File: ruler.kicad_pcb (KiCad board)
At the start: 2 copper layers, 170.8 x 38.1 mm, 80 parts, among them J1 USB_OTG, Q1 SOT23, Q2 SOT323, Q3 SOT883, Q4 SOT523, Q5 SOT223, Q6 SOT89, Q7 SuperSOT, SW1 KMR2, SW2 EVQPE1, SW3 B3U1000P, SW4 FSMCT, SW5 TL3315, SW6 FSM2JSM, SW7 JS202011SCQN, U1 QFN-0.5mm, U10 SOT963-6, U11 SSOP14, U12 SO16-L, U13 SOT666, U14 SOT1194, U15 SOT1333, U16 SOT669, U17 TSSOP 4.4x3mm, U18 SO4, U19 VSSOP, U2 LQFP, U3 SOIC, U4 BGA-0.8mm, U5 TSSOP 3x3mm, U6 MSOIC, U7 TSOP-0.95mm, U8 SOT23-6, U9 SOT23-8

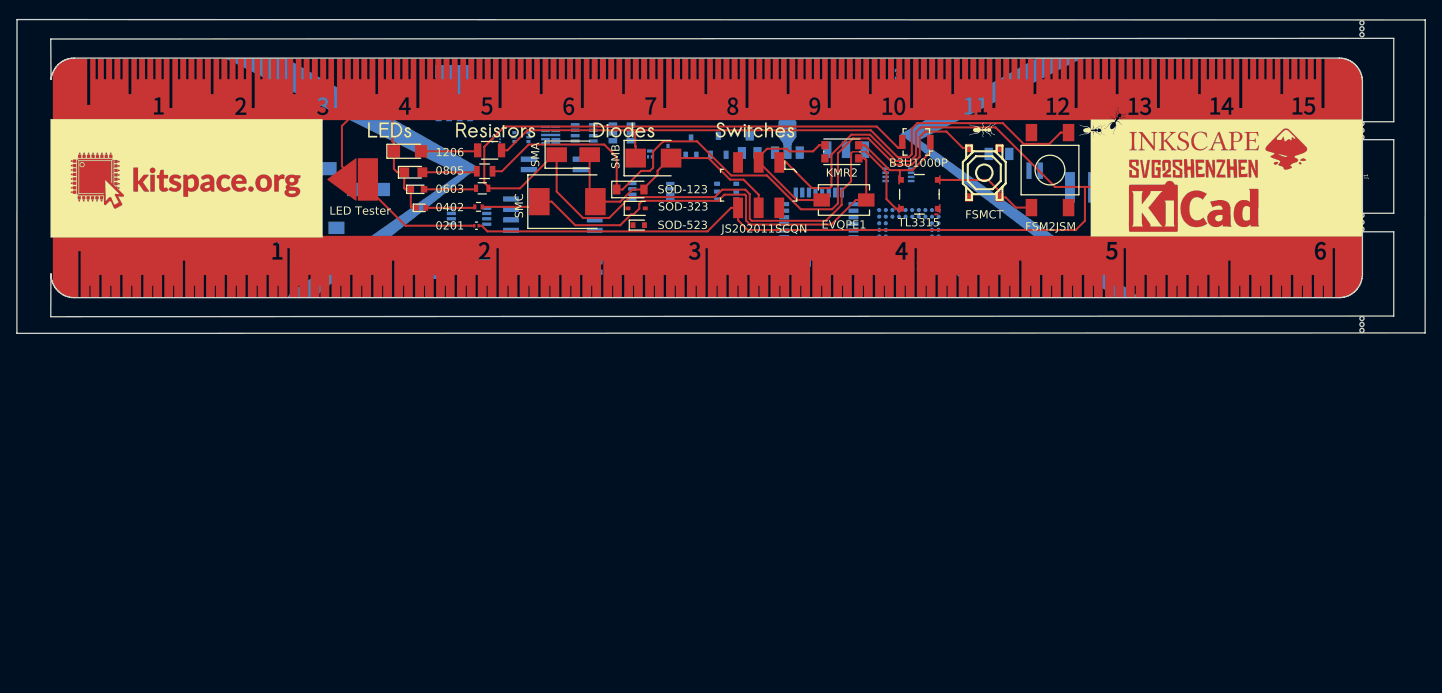
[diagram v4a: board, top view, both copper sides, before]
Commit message: Panelize two rulers
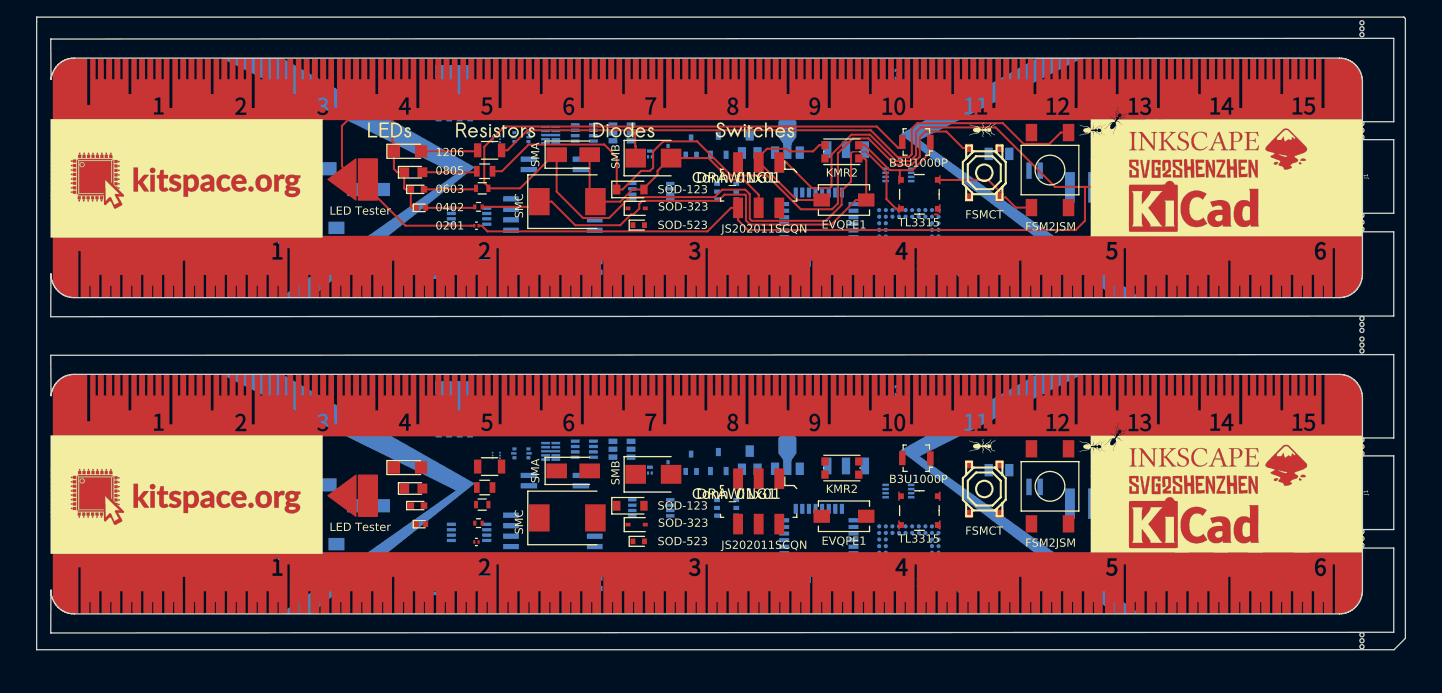
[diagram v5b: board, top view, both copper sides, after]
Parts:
- added C1: 3x5.3mm, KiCad/Capacitors_SMD.pretty:CP_Elec_3x5.3, B.Cu at (103.9, 144.8)
- added C2: 4x5.8mm, KiCad/Capacitors_SMD.pretty:CP_Elec_4x5.8, B.Cu at (96.9, 142.3)
- added C3: 5x5.8mm, KiCad/Capacitors_SMD.pretty:CP_Elec_5x5.8, B.Cu at (88.6, 140.0)
- added C4: 8x10mm, KiCad/Capacitors_SMD.pretty:CP_Elec_8x10, B.Cu at (78.2, 138.2)
- added C5: A/3216, KiCad/Capacitors_Tantalum_SMD.pretty:CP_Tantalum_Case-A_EIA-3216-18_Reflow, B.Cu at (98.6, 149.4)
- added C6: B/3528, KiCad/Capacitors_Tantalum_SMD.pretty:CP_Tantalum_Case-B_EIA-3528-21_Reflow, B.Cu at (92.3, 150.1)
- added C7: C/6032, KiCad/Capacitors_Tantalum_SMD.pretty:CP_Tantalum_Case-C_EIA-6032-28_Reflow, B.Cu at (84.6, 150.6)
- added C8: D/7343, KiCad/Capacitors_Tantalum_SMD.pretty:CP_Tantalum_Case-D_EIA-7343-31_Reflow, B.Cu at (74.9, 151.1)
- added D1: SMA, KiCad/Diodes_SMD.pretty:D_SMA, F.Cu at (128.7, 140.6)
- added D2: SMB, KiCad/Diodes_SMD.pretty:D_SMB, F.Cu at (138.4, 141.0)
- added D3: SMC, KiCad/Diodes_SMD.pretty:D_SMC, F.Cu at (128.0, 146.3)
- added D4: SOD-123, KiCad/Diodes_SMD.pretty:D_SOD-123, F.Cu at (135.6, 144.8)
- added D5: SOD-323, KiCad/Diodes_SMD.pretty:D_SOD-323, F.Cu at (136.4, 147.1)
- added D6: SOD-523, KiCad/Diodes_SMD.pretty:D_SOD-523, F.Cu at (136.7, 149.1)
- added DRAWING1: Conn_01x01, drawings:ruler, F.Cu at (148.5, 143.4)
- added DRAWING10: Conn_01x01, drawings:tantalum_text, B.Cu at (68.6, 152.7)
- added DRAWING11: Conn_01x01, drawings:electrolytic_text, B.Cu at (71.6, 139.4)
- added DRAWING12: Conn_01x01, drawings:vscore, B.Cu at (65.3, 136.4)
- added DRAWING13: Conn_01x01, drawings:mouse_bites, B.Cu at (213.4, 132.1)
- added DRAWING14: Conn_01x01, drawings:mouse, B.Cu at (188.7, 139.2)
- added DRAWING15: Conn_01x01, drawings:chipmunk, B.Cu at (202.7, 134.9)
- added DRAWING16: Conn_01x01, drawings:weasel, B.Cu at (214.4, 136.9)
- added DRAWING17: Conn_01x01, drawings:ant, B.Cu at (109.0, 159.3)
- added DRAWING18: Conn_01x01, drawings:ant, B.Cu at (177.5, 128.8)
- added DRAWING6: Conn_01x01, drawings:capacitors_text, B.Cu at (73.4, 131.1)
- added DRAWING9: Conn_01x01, drawings:inductors_text, B.Cu at (219.7, 146.8)
- added J1: USB_OTG, smisioto.eu/kicad_libs/modules/w_conn_pc.pretty:conn_usb_B_micro_smd, F.Cu at (222.2, 143.2)
- added L1: 1008, jnedbal/jakub.pretty:Inductor_1008, B.Cu at (180.3, 140.5)
- added L2: 8x8mm, KiCad/Inductors.pretty:Inductor_Taiyo-Yuden_NR-80xx, B.Cu at (214.3, 150.9)
- added L3: 4x4mm, KiCad/Inductors.pretty:Inductor_Taiyo-Yuden_MD-4040, B.Cu at (190.3, 144.5)
- added L4: 5x5mm, KiCad/Inductors.pretty:Inductor_Taiyo-Yuden_MD-5050, B.Cu at (197.6, 146.4)
- added L5: 6x6mm, KiCad/Inductors.pretty:Inductor_Taiyo-Yuden_NR-60xx, B.Cu at (204.9, 148.4)
- added L6: 2x2mm, KiCad/Inductors.pretty:Inductor_Taiyo-Yuden_NR-20xx, B.Cu at (184.7, 142.5)
- added LED1: LED Tester, custom:led_test_pads, F.Cu at (102.5, 143.6)
- added LED2: 0402, KiCad/LEDs.pretty:LED_0402, F.Cu at (110.3, 147.0)
- added LED3: 0603, KiCad/LEDs.pretty:LED_0603, F.Cu at (109.8, 144.8)
- added LED4: 0805, KiCad/LEDs.pretty:LED_0805, F.Cu at (109.3, 142.7)
- added LED5: 1206, KiCad/LEDs.pretty:LED_1206, F.Cu at (108.6, 140.1)
- added Q1: SOT23, adamgreig/agg-kicad/agg.pretty:SOT-23, B.Cu at (146.3, 139.4)
- added Q2: SOT323, adamgreig/agg-kicad/agg.pretty:SOT-323, B.Cu at (143.0, 139.6)
- added Q3: SOT883, adamgreig/agg-kicad/agg.pretty:SOT-883-B, B.Cu at (138.0, 140.5)
- added Q4: SOT523, digikey/digikey-kicad-library/digikey-footprints.pretty:SOT-523, B.Cu at (140.2, 140.8)
- added Q5: SOT223, ep092/library_toni.pretty:SOT223_GND_VO_VI, B.Cu at (161.8, 136.7)
- added Q6: SOT89, KiCad/TO_SOT_Packages_SMD.pretty:SOT-89-3, B.Cu at (154.7, 138.8)
- added Q7: SuperSOT, KiCad/TO_SOT_Packages_SMD.pretty:SuperSOT-3, B.Cu at (150.1, 139.3)
- added R1: 1k, KiCad/Resistors_SMD.pretty:R_0201, F.Cu at (117.0, 149.2)
- added R2: 1k, KiCad/Resistors_SMD.pretty:R_0402, F.Cu at (117.2, 146.9)
- added R3: 1k, KiCad/Resistors_SMD.pretty:R_0603, F.Cu at (117.7, 144.6)
- added R4: 1k, KiCad/Resistors_SMD.pretty:R_0805, F.Cu at (118.0, 142.6)
- added R5: 1k, KiCad/Resistors_SMD.pretty:R_1206, F.Cu at (118.6, 140.0)
- added SW1: KMR2, KiCad/Buttons_Switches_SMD.pretty:SW_SPST_KMR2, F.Cu at (161.3, 140.2)
- added SW2: EVQPE1, KiCad/Buttons_Switches_SMD.pretty:SW_SPST_EVQPE1, F.Cu at (161.5, 146.1)
- added SW3: B3U1000P, digikey/digikey-kicad-library/digikey-footprints.pretty:Switch_Tactile_SMD_B3U-1000P, F.Cu at (170.3, 139.0)
- added SW4: FSMCT, custom:FSMCT, F.Cu at (178.6, 142.7)
- added SW5: TL3315, digikey/digikey-kicad-library/digikey-footprints.pretty:Switch_4.5x4.5mm_SMD_TL3315NF160Q, F.Cu at (170.7, 145.4)
- added SW6: FSM2JSM, custom:FSM2JSMA, F.Cu at (186.5, 142.4)
- added SW7: JS202011SCQN, digikey/digikey-kicad-library/digikey-footprints.pretty:Switch_Slide_JS202011SCQN, F.Cu at (151.2, 144.3)
- added U1: QFN-0.5mm, KiCad/Housings_DFN_QFN.pretty:QFN-16-1EP_3x3mm_Pitch0.5mm, B.Cu at (148.1, 153.2)
- added U10: SOT963-6, KiCad/TO_SOT_Packages_SMD.pretty:SOT-963, B.Cu at (119.4, 138.7)
- added U11: SSOP14, KiCad/SMD_Packages.pretty:SSOP-14, B.Cu at (178.8, 153.2)
- added U12: SO16-L, KiCad/SMD_Packages.pretty:SO-16-L, B.Cu at (126.2, 150.4)
- added U13: SOT666, KiCad/TO_SOT_Packages_SMD.pretty:SOT-666, B.Cu at (122.4, 138.4)
- added U14: SOT1194, adamgreig/agg-kicad/agg.pretty:SOT-1194-1, B.Cu at (168.1, 130.8)
- added U15: SOT1333, KiCad/TO_SOT_Packages_SMD.pretty:SOT-1333-1, B.Cu at (126.0, 138.2)
- added U16: SOT669, KiCad/TO_SOT_Packages_SMD.pretty:SOT-669_LFPAK, B.Cu at (114.3, 133.1)
- added U17: TSSOP 4.4x3mm, KiCad/Housings_SSOP.pretty:TSSOP-8_4.4x3mm_Pitch0.65mm, B.Cu at (115.1, 154.4)
- added U18: SO4, KiCad/Housings_SOIC.pretty:SO-4_4.4x2.3mm_Pitch1.27mm, B.Cu at (126.5, 141.7)
- added U19: VSSOP, KiCad/Housings_SSOP.pretty:VSSOP-8_2.3x2mm_Pitch0.5mm, B.Cu at (168.1, 143.0)
- added U2: LQFP, adamgreig/agg-kicad/agg.pretty:LQFP-32, B.Cu at (158.5, 149.4)
- added U3: SOIC, adamgreig/agg-kicad/agg.pretty:SOIC-8, B.Cu at (138.7, 152.9)
- added U4: BGA-0.8mm, KiCad/SMD_Packages.pretty:BGA-64-0.8mm, B.Cu at (169.4, 150.9)
- added U5: TSSOP 3x3mm, KiCad/Housings_SSOP.pretty:TSSOP-8_3x3mm_Pitch0.65mm, B.Cu at (116.1, 148.0)
- added U6: MSOIC, smisioto.eu/kicad_libs/modules/w_smd_dil.pretty:msoic-8, B.Cu at (138.2, 145.0)
- added U7: TSOP-0.95mm, KiCad/Housings_SSOP.pretty:TSOP-6_1.65x3.05mm_Pitch0.95mm, B.Cu at (147.3, 145.0)
- added U8: SOT23-6, KiCad/TO_SOT_Packages_SMD.pretty:SOT-23-6, B.Cu at (134.6, 137.9)
- added U9: SOT23-8, KiCad/TO_SOT_Packages_SMD.pretty:SOT-23-8, B.Cu at (130.0, 137.9)
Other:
- board size 170.8 x 38.1 mm -> 166 x 76.7 mm
- board text added: "Please only add serial numbers to frame."
- board text added: "V-SCORE"

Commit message: Make adjustements for AllPCB panelization
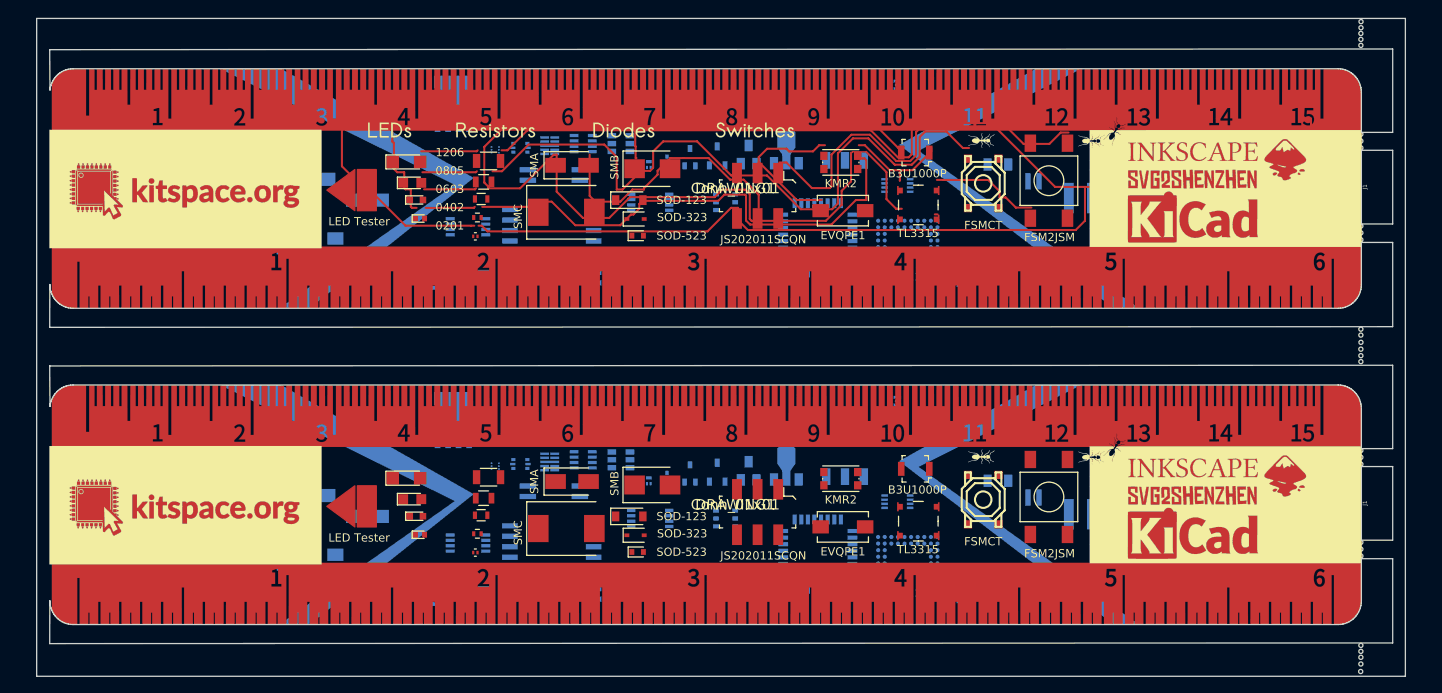
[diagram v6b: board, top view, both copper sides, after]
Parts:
- moved Q3 1.30 mm to (137.9, 141.8)
- moved SW4 1.30 mm to (178.4, 144.0)
- moved DRAWING6 1.30 mm to (73.3, 132.4)
- moved LED1 1.30 mm to (102.3, 144.9)
- moved R5 1.30 mm to (118.4, 141.3)
- moved C2 1.30 mm to (96.8, 143.5)
- moved C4 1.30 mm to (78.1, 139.5)
- moved D3 1.30 mm to (127.9, 147.5)
- moved DRAWING1 1.30 mm to (148.4, 144.6)
- moved DRAWING18 1.30 mm to (177.4, 130.1)
- moved L1 1.30 mm to (180.2, 141.8)
- moved L4 1.30 mm to (197.5, 147.7)
- moved L5 1.30 mm to (204.8, 149.7)
- moved LED4 1.30 mm to (109.2, 144.0)
- moved Q5 1.30 mm to (161.7, 137.9)
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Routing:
- net Net-(D2-Pad1): track 79.8 -> 162.8 mm
- net Net-(D4-Pad1): track 83.0 -> 0.00 mm
- net (no net): track 0.00 -> 6.85 mm
- net GND: track 33.8 -> 26.9 mm
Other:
- board size 166 x 76.7 mm -> 166 x 79.8 mm

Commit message: Remove second copy for now, remove all tracks
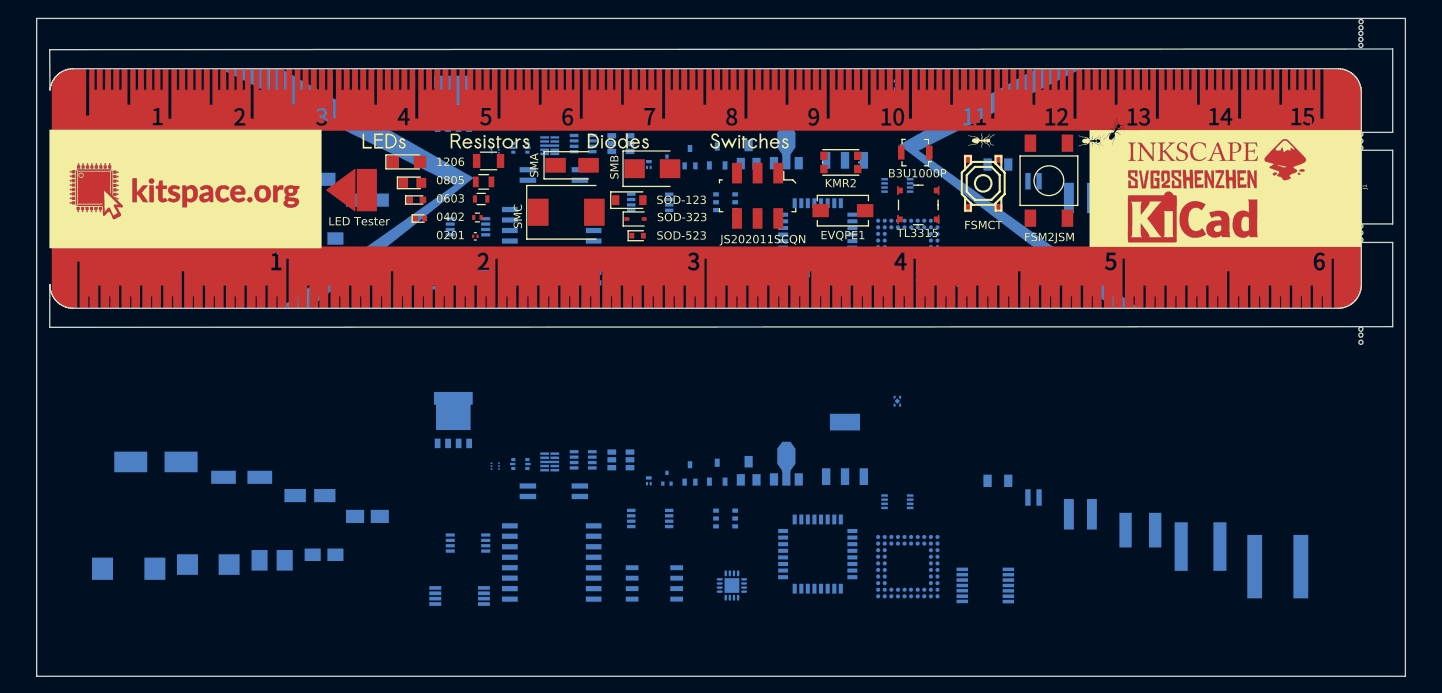
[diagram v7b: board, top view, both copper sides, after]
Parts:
- removed the D1 at (128.6, 141.8)
- removed the D2 at (138.3, 142.3)
- removed the D3 at (127.9, 147.5)
- removed the D4 at (135.5, 146.1)
- removed the D5 at (136.3, 148.4)
- removed the D6 at (136.5, 150.4)
- removed the DRAWING1 at (148.4, 144.6)
- removed the J1 at (222.1, 144.5)
- removed the LED1 at (102.3, 144.9)
- removed the LED2 at (110.1, 148.3)
- removed the LED3 at (109.7, 146.0)
- removed the LED4 at (109.2, 144.0)
- removed the LED5 at (108.5, 141.4)
- removed the R1 at (116.8, 150.5)
- removed the R2 at (117.1, 148.2)
- removed the R3 at (117.5, 145.9)
- removed the R4 at (117.8, 143.9)
- removed the R5 at (118.4, 141.3)
- removed the SW1 at (161.2, 141.5)
- removed the SW2 at (161.4, 147.3)
- removed the SW3 at (170.2, 140.3)
- removed the SW4 at (178.4, 144.0)
- removed the SW5 at (170.6, 146.7)
- removed the SW6 at (186.4, 143.7)
- removed the SW7 at (151.1, 145.5)
- moved DRAWING3 1.50 mm to (119.5, 100.9)
- moved DRAWING2 1.50 mm to (114.7, 99.6)
- moved DRAWING4 1.50 mm to (134.2, 100.9)
- moved DRAWING5 1.50 mm to (151.0, 100.9)
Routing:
- net Net-(D2-Pad1): track 162.8 -> 0.00 mm
- net +5V: track 161.3 -> 0.00 mm
- net Net-(D1-Pad1): track 132.2 -> 0.00 mm
- net Net-(D3-Pad1): track 60.2 -> 0.00 mm
- net SW_V+: track 45.1 -> 0.00 mm
- net LED_V+: track 31.8 -> 0.00 mm
- net GND: track 26.9 -> 0.00 mm
- net Net-(LED1-Pad2): track 16.0 -> 0.00 mm
- net Net-(LED5-Pad2): track 6.91 -> 0.00 mm
- net Net-(LED4-Pad2): track 6.66 -> 0.00 mm
- net Net-(LED3-Pad2): track 6.36 -> 0.00 mm
- net Net-(LED2-Pad2): track 6.01 -> 0.00 mm
